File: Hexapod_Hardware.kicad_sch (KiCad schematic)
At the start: 2 parts, among them J1 Conn_01x05_Pin, J2 Conn_01x04_Socket

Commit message: ordered pcbs
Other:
- moved on the sheet: J1, J2

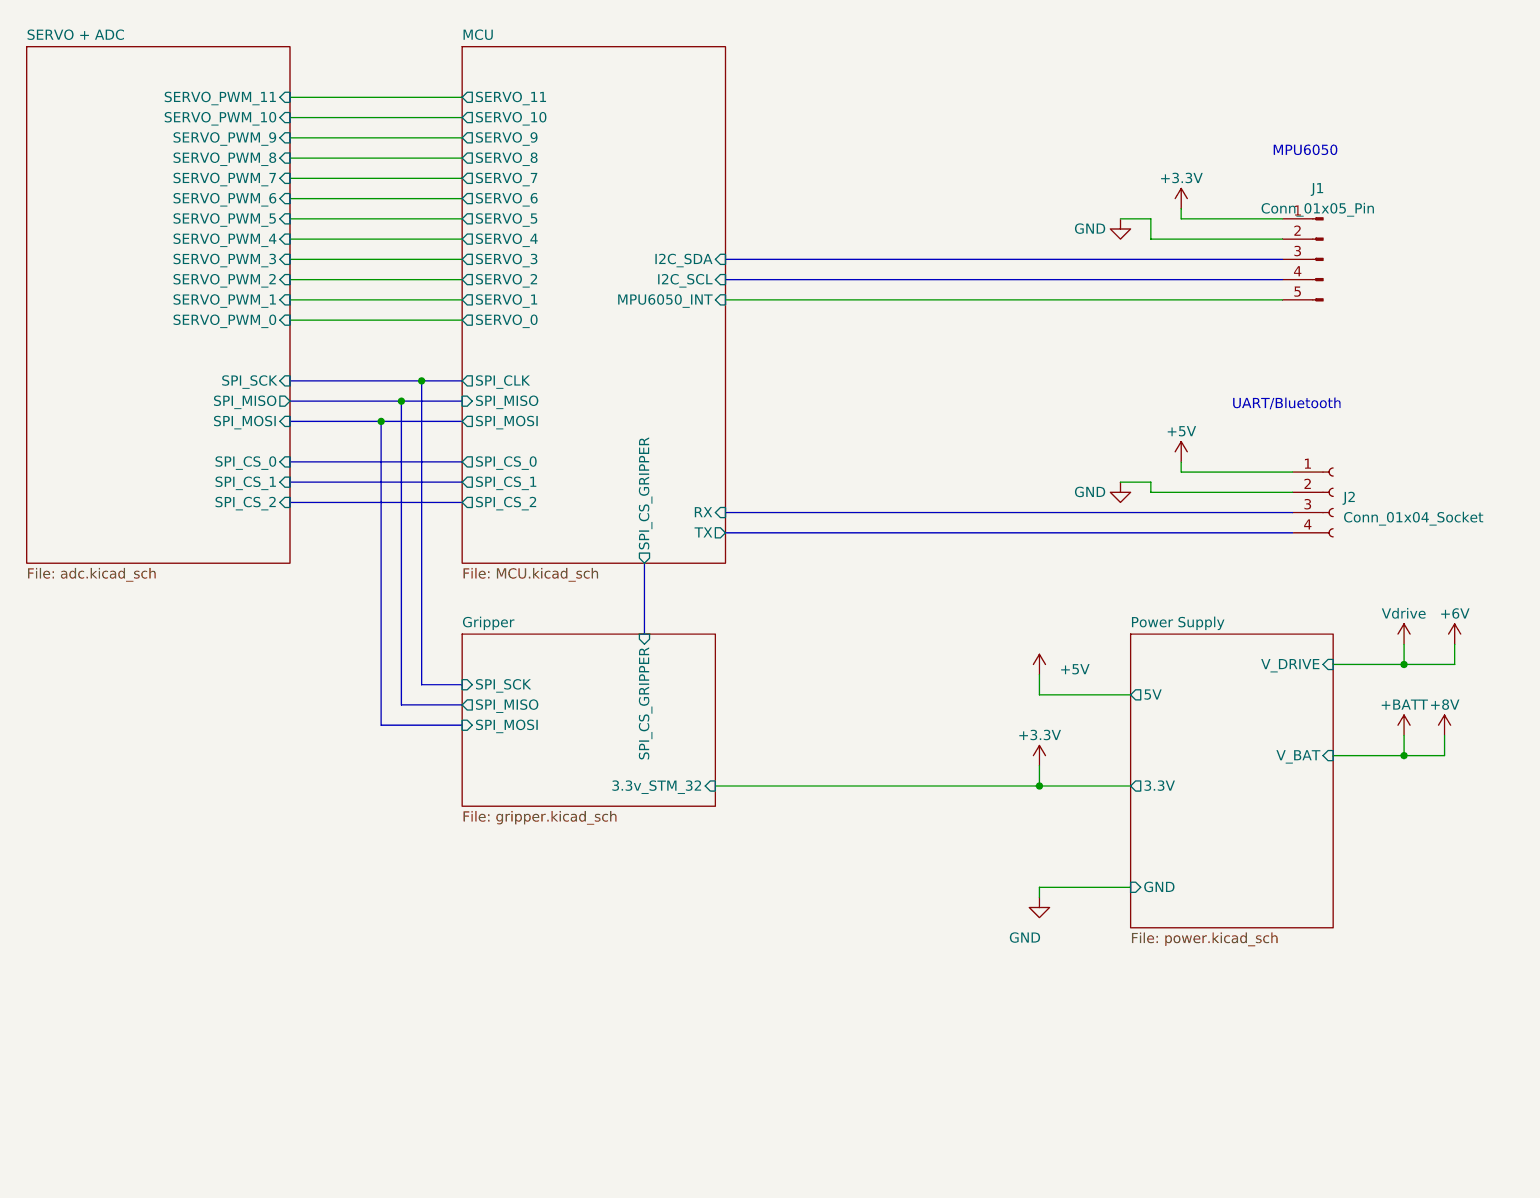
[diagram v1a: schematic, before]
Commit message: Bord v1.2, added flash memory, changed pinout od servomotor connectors and removed potentiometer signal from servomotors plus one ADC
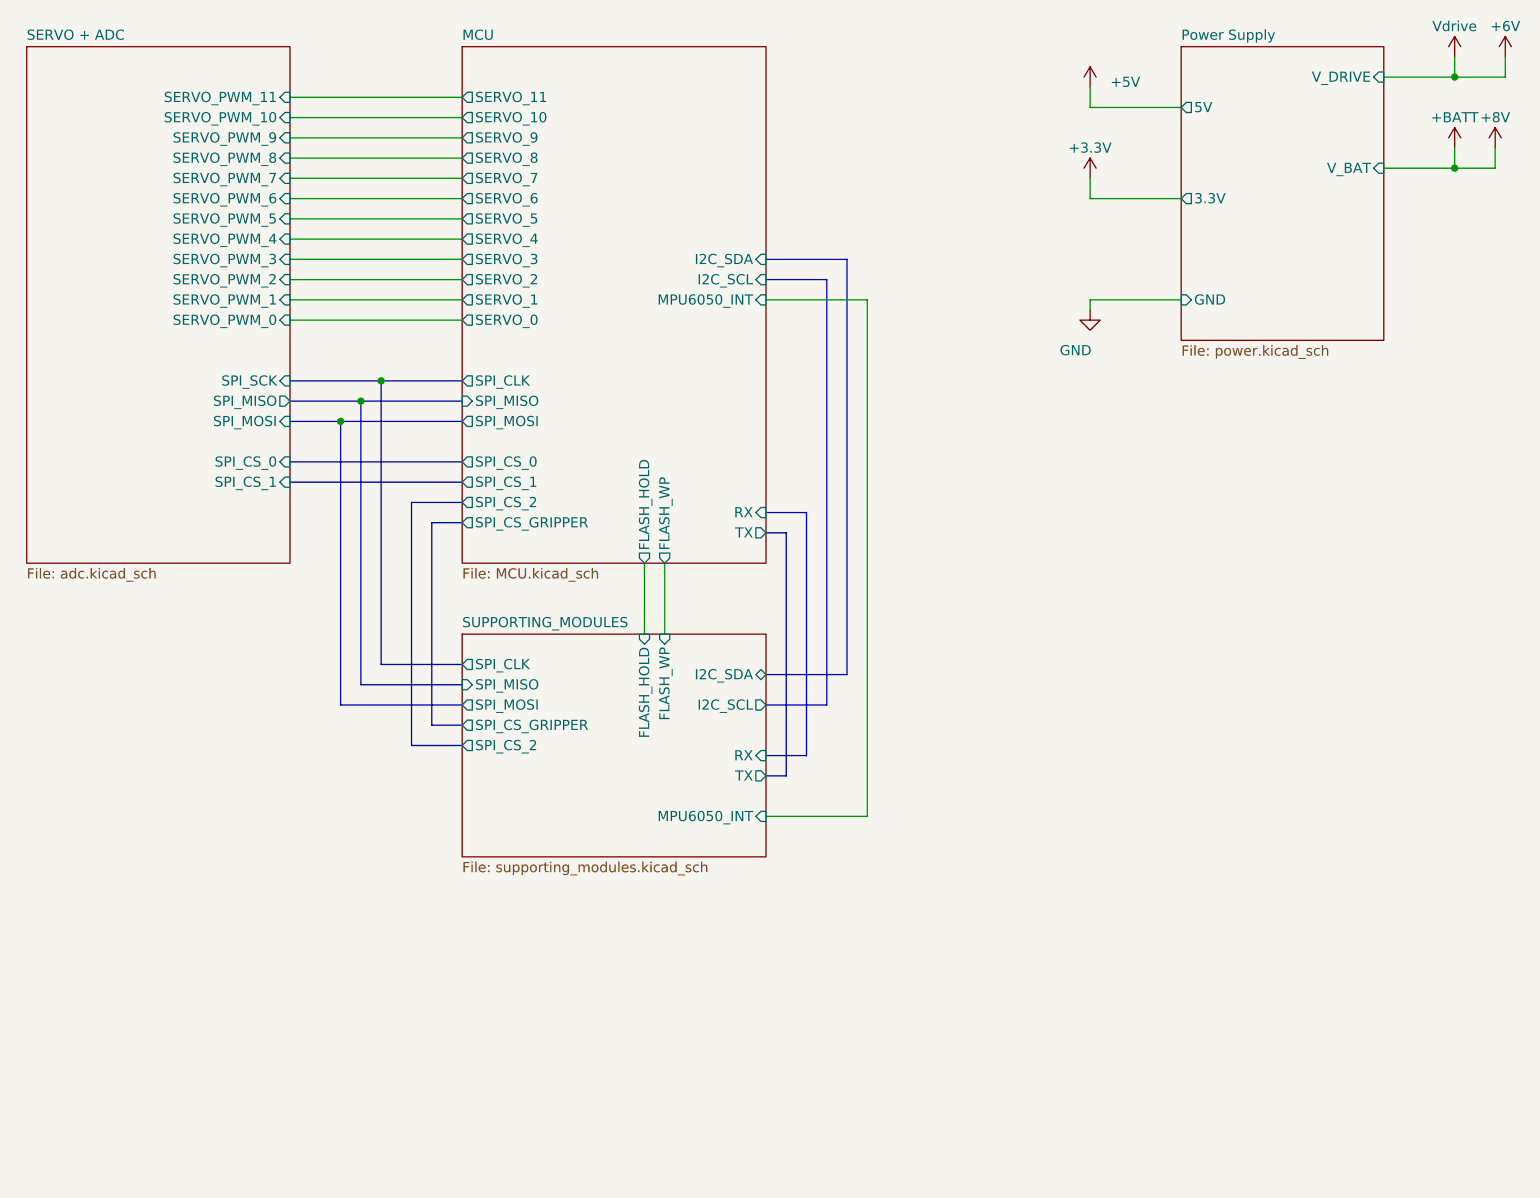
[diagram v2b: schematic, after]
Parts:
- removed J1: Conn_01x05_Pin, Connector_PinSocket_2.54mm:PinSocket_1x05_P2.54mm_Vertical, symbol Connector:Conn_01x05_Pin
- removed J2: Conn_01x04_Socket, Connector_PinHeader_2.54mm:PinHeader_1x04_P2.54mm_Vertical, symbol Connector:Conn_01x04_Socket
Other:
- removed sheet Gripper
- added sheet SUPPORTING_MODULES (supporting_modules.kicad_sch)
- sheet MCU ports: added FLASH_HOLD, FLASH_WP; removed none
- sheet SERVO + ADC ports: added none; removed SPI_CS_2
- note removed: "MPU6050"
- note removed: "UART/Bluetooth"
